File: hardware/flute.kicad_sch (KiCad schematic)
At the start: 0 parts

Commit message: r and c footprint change
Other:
- sheet RASPBERRY_PI_PICO ports: added GPIO0, GPIO1, GPIO10, GPIO11, GPIO12, GPIO13, GPIO14, GPIO15, GPIO16, GPIO17, GPIO18, GPIO19, GPIO2, GPIO20, GPIO21, GPIO22, GPIO23, GPIO24, GPIO25, GPIO26, GPIO27, GPIO28, GPIO29, GPIO3, GPIO4, GPIO5, GPIO6, GPIO7, GPIO8, GPIO9; removed none

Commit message: minor schematic changes
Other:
- sheet RASPBERRY_PI_PICO ports: added none; removed GPIO0, GPIO1, GPIO10, GPIO11, GPIO12, GPIO13, GPIO14, GPIO15, GPIO16, GPIO17, GPIO18, GPIO19, GPIO2, GPIO20, GPIO21, GPIO22, GPIO23, GPIO24, GPIO25, GPIO26, GPIO27, GPIO28, GPIO29, GPIO3, GPIO4, GPIO5, GPIO6, GPIO7, GPIO8, GPIO9
- note added: "RASPBERRY_PI_PICO"
- note removed: "RASPBERRY_PI_PIKO"

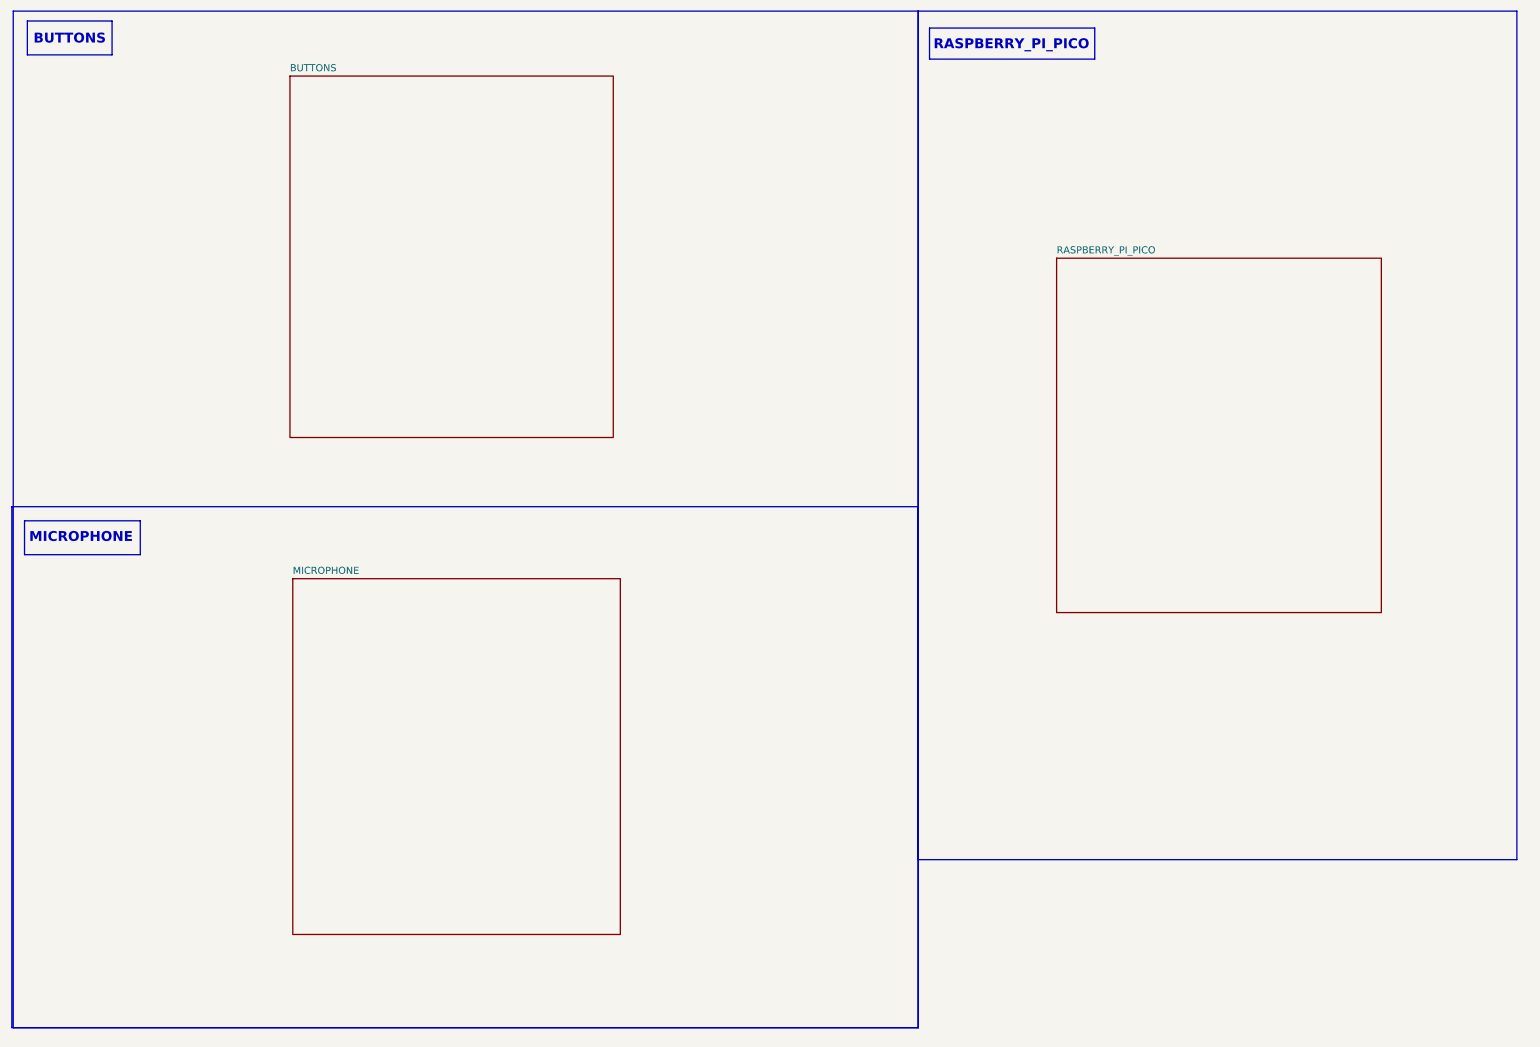
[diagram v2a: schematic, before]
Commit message: added jack and battery
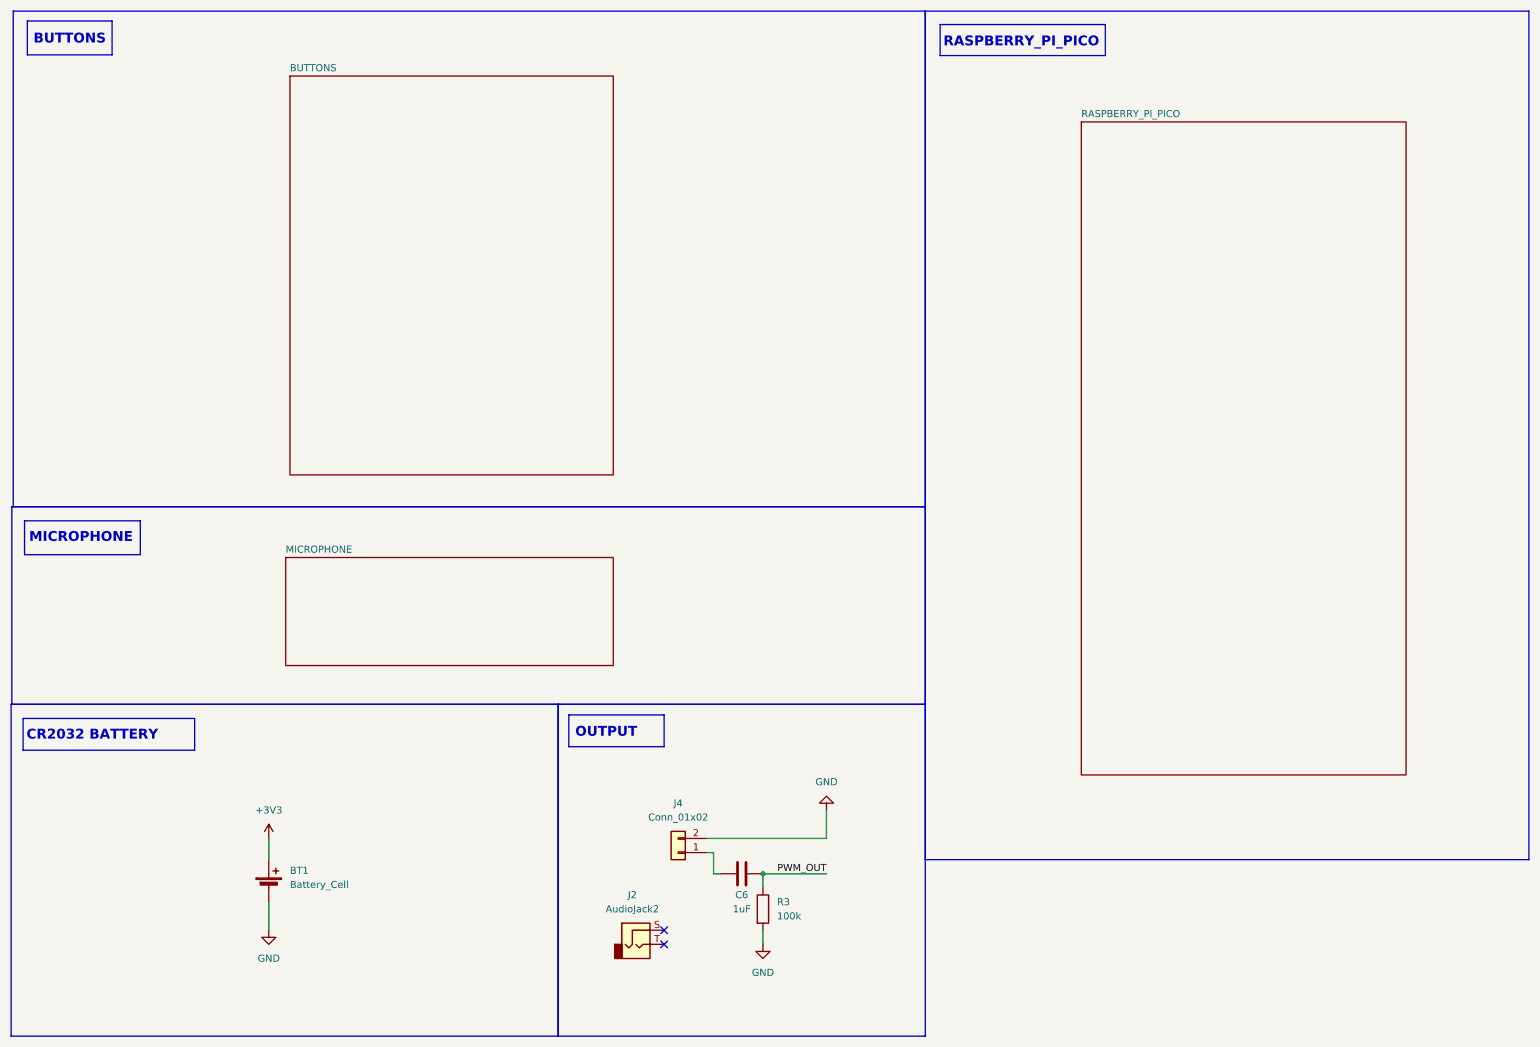
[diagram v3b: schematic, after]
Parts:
- added BT1: Battery_Cell, Battery:BatteryHolder_MYOUNG_BS-07-A1BJ001_CR2032, symbol Device:Battery_Cell
- added C6: 1uF, Capacitor_SMD:C_0603_1608Metric, symbol Device:C
- added J2: AudioJack2, symbol Connector_Audio:AudioJack2
- added J4: Conn_01x02, Connector_PinHeader_2.54mm:PinHeader_1x02_P2.54mm_Vertical, symbol Connector_Generic:Conn_01x02
- added R3: 100k, Resistor_SMD:R_0603_1608Metric, symbol Device:R
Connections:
- new net: C6.1, J4.1 (Pin_1)
- new net +3V3: BT1.1 (+)
- new net GND: BT1.2 (-), J4.2 (Pin_2), R3.2
- new net PWM_OUT: C6.2, R3.1
- no-connect marks 0 -> 2
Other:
- note added: "CR2032 BATTERY"
- note added: "OUTPUT"

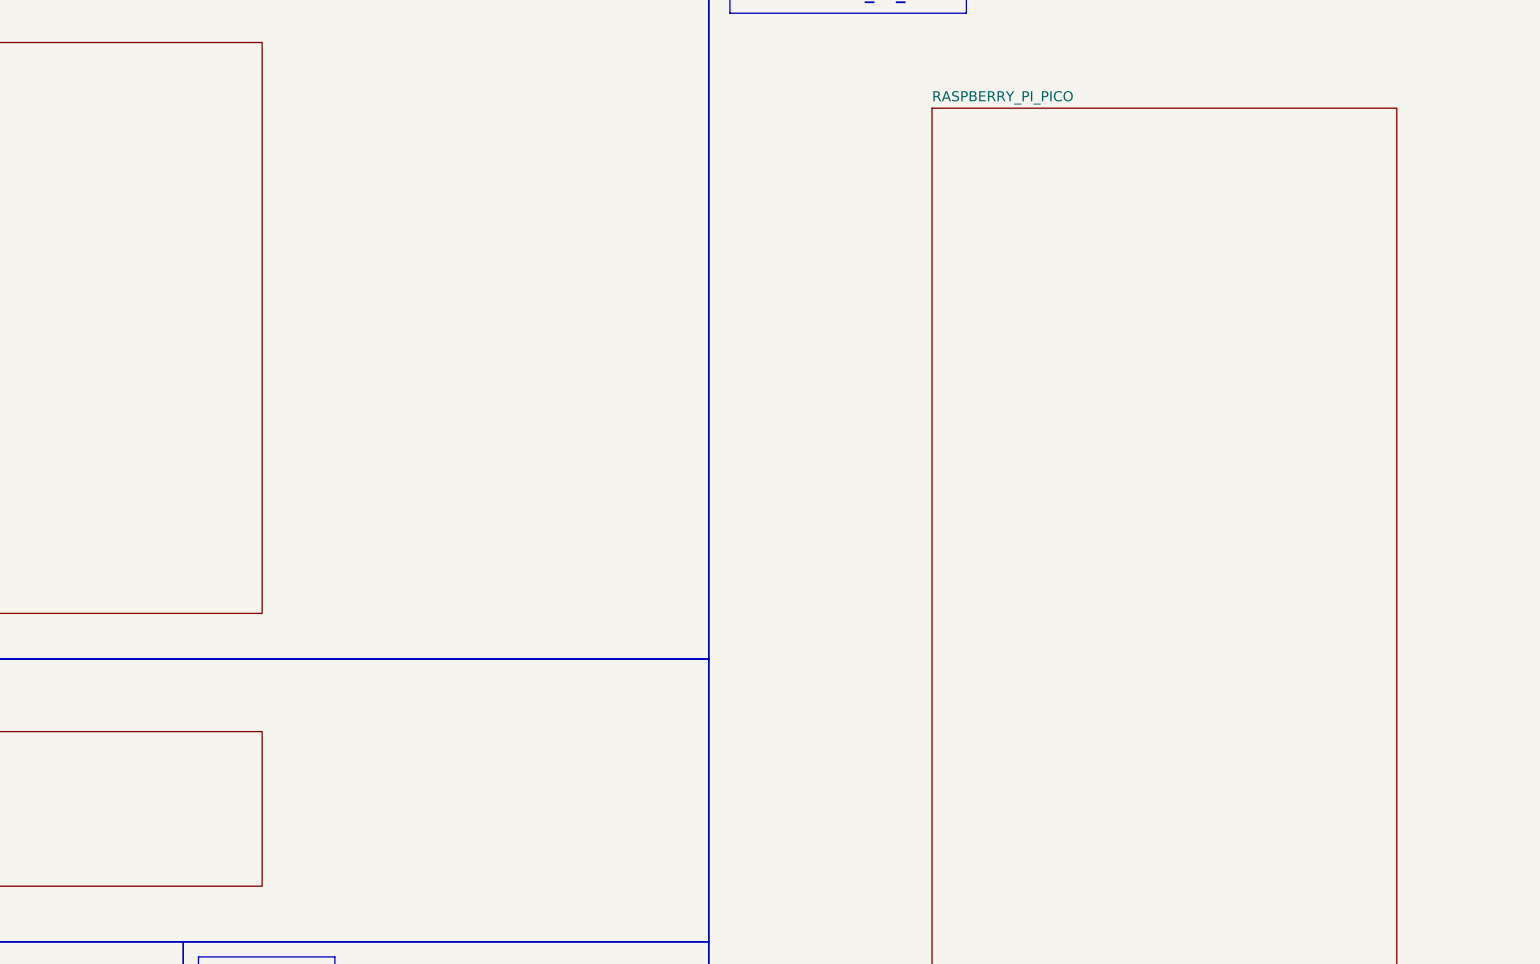
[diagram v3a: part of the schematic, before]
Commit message: type of connections changed
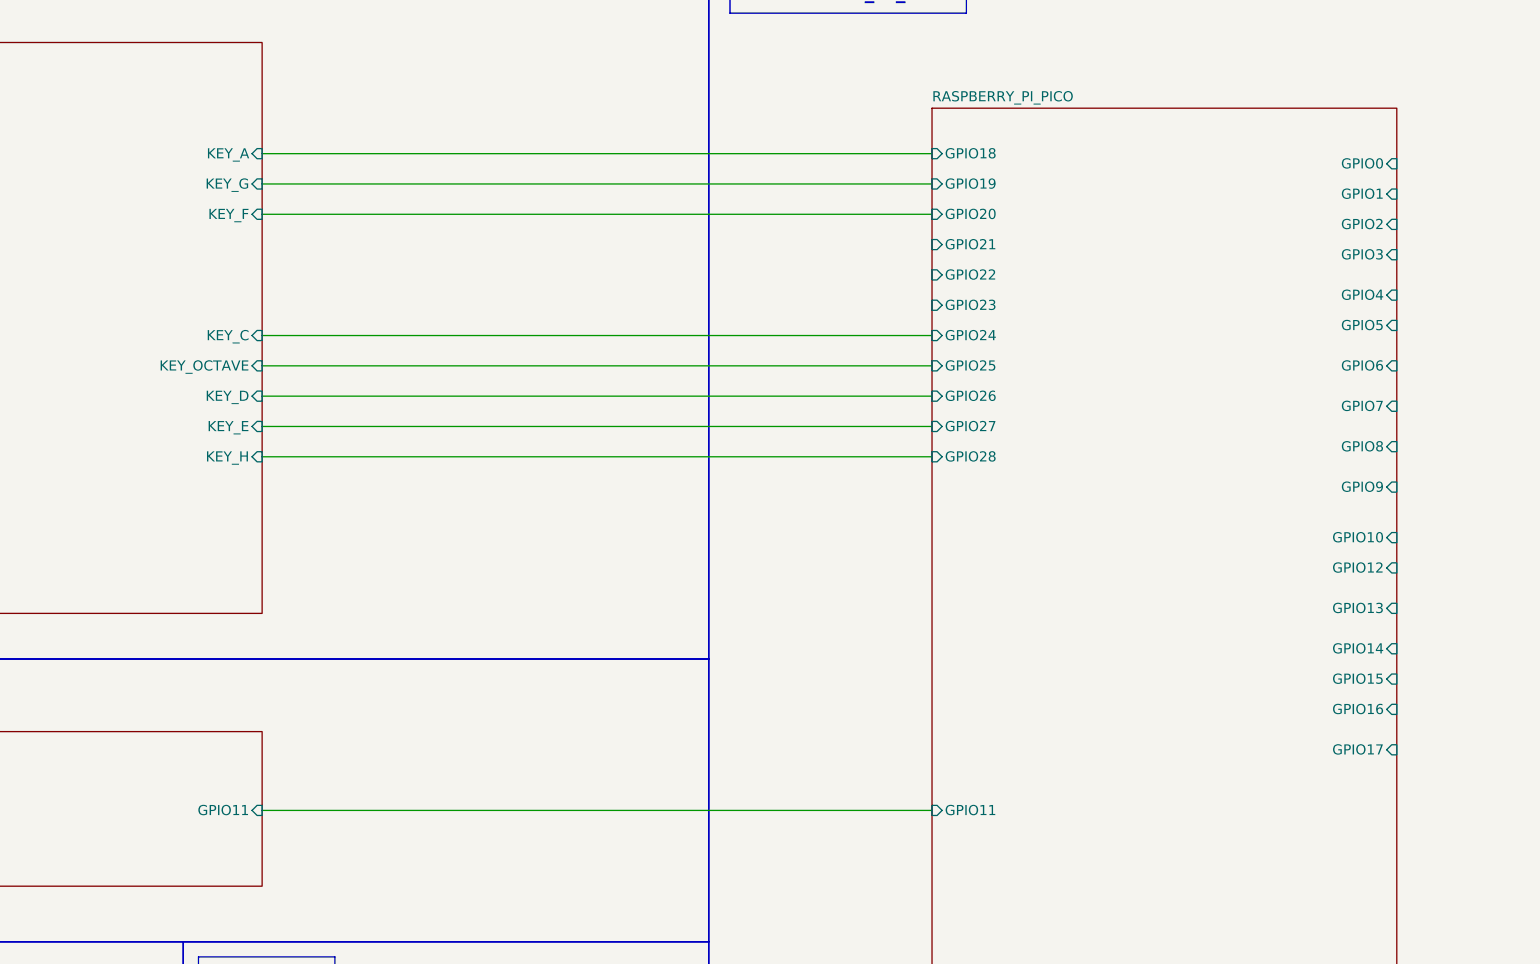
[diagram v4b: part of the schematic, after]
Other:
- sheet BUTTONS ports: added KEY_A, KEY_C, KEY_D, KEY_E, KEY_F, KEY_G, KEY_H, KEY_OCTAVE; removed none
- sheet MICROPHONE ports: added GPIO11; removed none
- sheet RASPBERRY_PI_PICO ports: added GPIO0, GPIO1, GPIO10, GPIO11, GPIO12, GPIO13, GPIO14, GPIO15, GPIO16, GPIO17, GPIO18, GPIO19, GPIO2, GPIO20, GPIO21, GPIO22, GPIO23, GPIO24, GPIO25, GPIO26, GPIO27, GPIO28, GPIO3, GPIO4, GPIO5, GPIO6, GPIO7, GPIO8, GPIO9; removed none

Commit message: complete pcb ver1
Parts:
- added C2: 1uF, Capacitor_SMD:C_0603_1608Metric, symbol Device:C
- added MIC.CASE1: R, Resistor_THT:R_Axial_DIN0204_L3.6mm_D1.6mm_P2.54mm_Vertical, symbol Device:R
- added R2: 2.2K, Resistor_SMD:R_0603_1608Metric, symbol Device:R
- added SW1: C, Button_Switch_THT:SW_TH_Tactile_Omron_B3F-100x, symbol Switch:SW_Omron_B3FS
- added SW2: D, Button_Switch_THT:SW_TH_Tactile_Omron_B3F-100x, symbol Switch:SW_Omron_B3FS
- added SW3: E, Button_Switch_THT:SW_TH_Tactile_Omron_B3F-100x, symbol Switch:SW_Omron_B3FS
- added SW4: F, Button_Switch_THT:SW_TH_Tactile_Omron_B3F-100x, symbol Switch:SW_Omron_B3FS
- added SW5: G, Button_Switch_THT:SW_TH_Tactile_Omron_B3F-100x, symbol Switch:SW_Omron_B3FS
- added SW6: A, Button_Switch_THT:SW_TH_Tactile_Omron_B3F-100x, symbol Switch:SW_Omron_B3FS
- added SW7: H, Button_Switch_THT:SW_TH_Tactile_Omron_B3F-100x, symbol Switch:SW_Omron_B3FS
- added SW8: OCTAVE?, Button_Switch_THT:SW_TH_Tactile_Omron_B3F-100x, symbol Switch:SW_Omron_B3FS
- renumbered C6 to C1, J2 to J1, J4 to J2, R3 to R1
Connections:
- net +3V3: now also R2.2
- net GND: now also MIC.CASE1.1, SW1.1, SW2.1, SW3.1, SW4.1, SW5.1, SW6.1, SW7.1, SW8.1
- new net: C2.1, MIC.CASE1.2, R2.1
- new net KEY_A: SW6.2
- new net KEY_C: SW1.2
- new net KEY_D: SW2.2
- new net KEY_E: SW3.2
- new net KEY_F: SW4.2
- new net KEY_G: SW5.2
- new net KEY_H: SW7.2
- new net KEY_OCTAVE: SW8.2
- new net MIC_OUTPUT: C2.2
- no-connect marks 2 -> 22
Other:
- removed sheet BUTTONS
- removed sheet MICROPHONE
- sheet RASPBERRY_PI_PICO ports: added GPIO29; removed none
- company: (none) -> KN HARDWIRE AGH
- title: (none) -> ELECTRONIC FLUTE
